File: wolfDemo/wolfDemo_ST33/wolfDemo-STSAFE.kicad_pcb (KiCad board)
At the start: 2 copper layers, 25.4 x 28.6 mm, 13 parts, among them CON1 MIKROBUS_MODULE_CONN, IC1 ST33KTPM2I3WBZA9

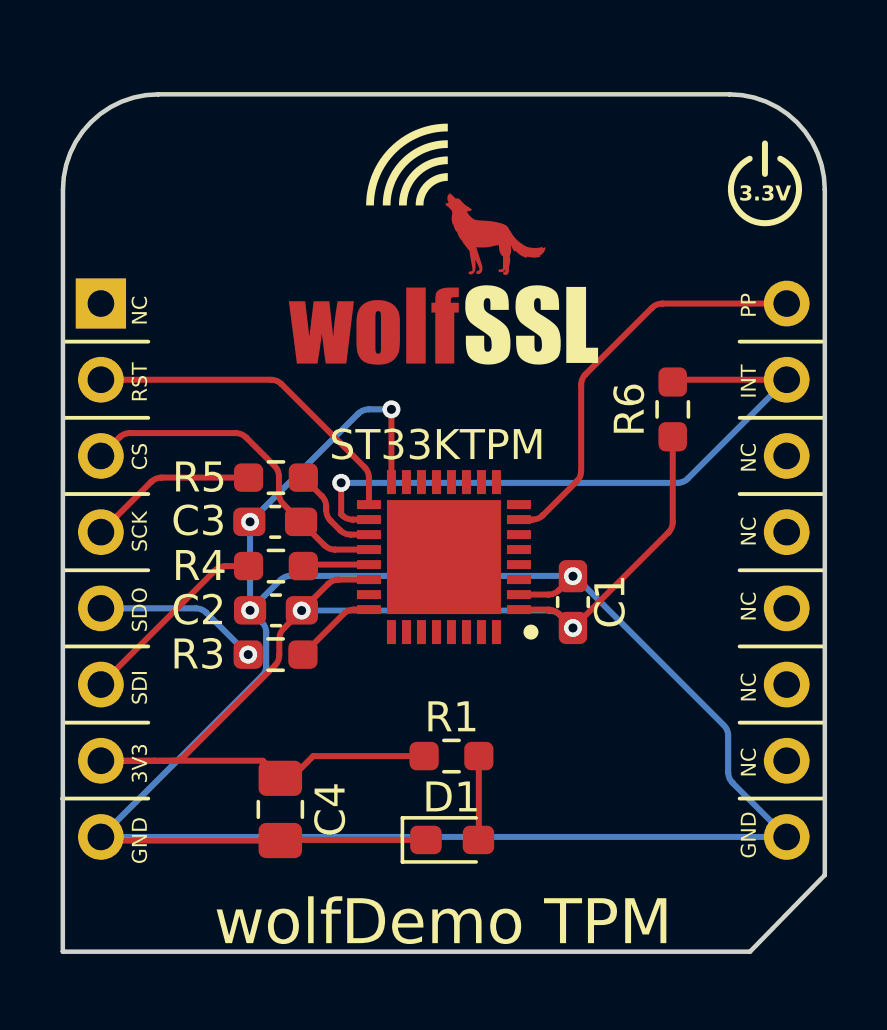
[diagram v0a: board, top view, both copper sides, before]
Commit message: Update board to 1.2
Also update README
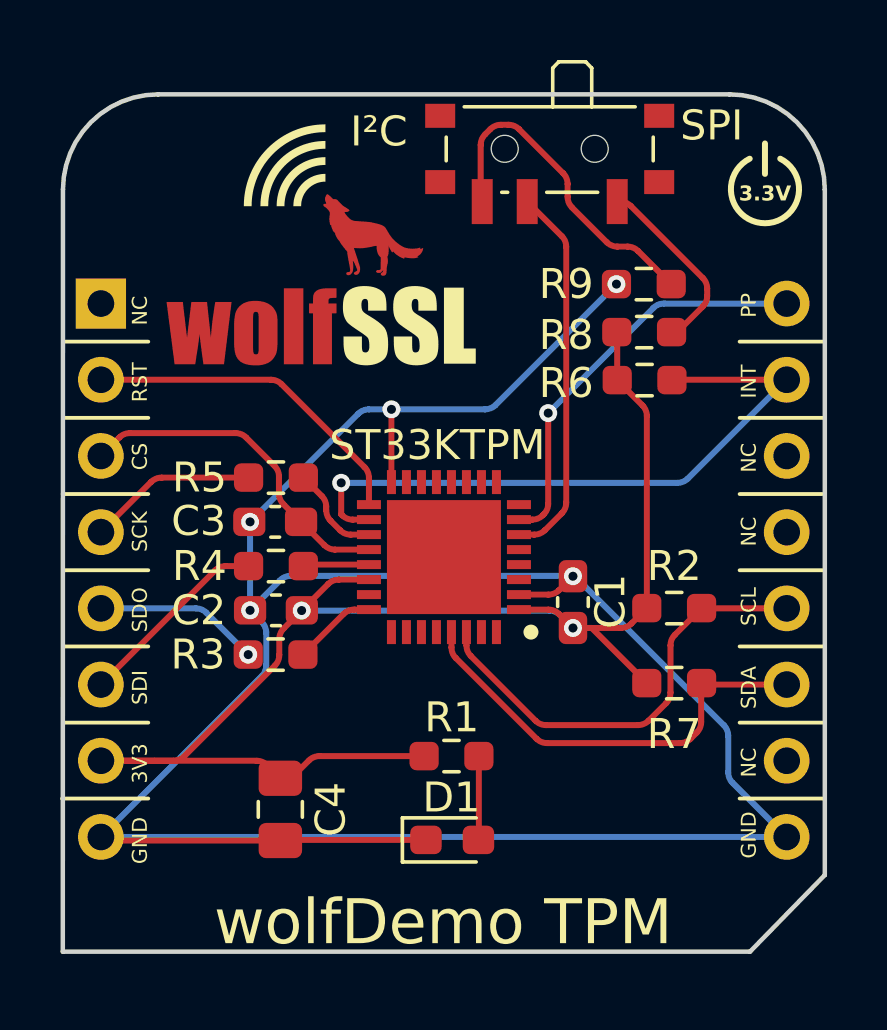
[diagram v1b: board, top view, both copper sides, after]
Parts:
- added R2: 1K, Resistor_SMD:R_0603_1608Metric_Pad0.98x0.95mm_HandSolder, F.Cu at (200.2, 81.3)
- added R7: 1K, Resistor_SMD:R_0603_1608Metric_Pad0.98x0.95mm_HandSolder, F.Cu at (200.2, 83.8)
- added R8: 4.7K, Resistor_SMD:R_0603_1608Metric_Pad0.98x0.95mm_HandSolder, F.Cu at (199.2, 72.1)
- added R9: 4.7K, Resistor_SMD:R_0603_1608Metric_Pad0.98x0.95mm_HandSolder, F.Cu at (199.2, 70.5)
- added SW1: SW_SPDT, Button_Switch_SMD:SW_SPDT_PCM12, F.Cu at (196.1, 66.3)
- R1: value R -> 470
- moved R6 1.35 mm to (199.2, 73.7), turned to 0 degrees
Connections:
- CON1 pad P11: unconnected-(CON1-SDA-PadP11) -> /SDA
- CON1 pad P12: unconnected-(CON1-SCL-PadP12) -> /SCL
- IC1 pad 29: unconnected-(IC1-2C_SDA/GPIO_6-Pad29) -> /SDA
- IC1 pad 30: unconnected-(IC1-I2C_SCL/GPIO_5-Pad30) -> /SCL
- IC1 pad 6: unconnected-(IC1-GPI_I2C_SELECT-Pad6) -> /I2CSEL
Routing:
- net /SCL: track 0.00 -> 15.0 mm
- net /SDA: track 0.00 -> 14.8 mm
- net /I2CSEL: track 0.00 -> 12.6 mm
- net Net-(SW1-C): track 0.00 -> 11.2 mm
- net GND: track 80.3 -> 89.5 mm, vias 4 -> 5
- net +3.3V: track 42.2 -> 50.0 mm
- net Net-(SW1-A): track 0.00 -> 6.30 mm
- net /PP: vias 0 -> 1
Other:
- board text added: "HW REV. 1.1"
- board text added: "I²C"
- board text added: "SPI"
- board text removed: "HW REV. 1.00a"
